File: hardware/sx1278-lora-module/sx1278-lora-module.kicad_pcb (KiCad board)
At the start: 2 copper layers, 17 x 16.5 mm, 1 part, among them J1 Conn_01x16

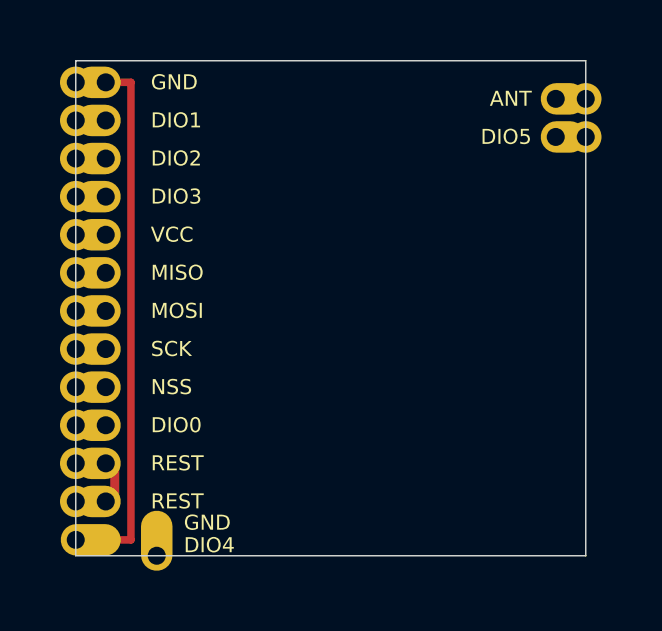
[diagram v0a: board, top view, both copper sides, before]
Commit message: SX1278 module: correct pad layout and pin names from the pinout photo
The seller's dimensioned pinout photo shows 12 keyhole pads along one
edge, two small castellation-only notches (DIO4, DIO5) on the adjacent
edge at the shared corner, and two keyhole pads (ANT, GND) at the
opposite corner.  Pin names in physical order are GND DIO1 DIO2 DIO3
VCC MISO MOSI SCK NSS DIO0 REST GND, DIO4 DIO5, GND ANT; the seller's
table duplicated REST and shifted its tail.  Positions re-measured
from the top-down photo: row holes 1.2 mm in from the edge starting
1.2 mm from the corner, notches at 1.25/2.7 mm, ANT/GND at 1.4/2.8 mm.

Co-Authored-By: Claude Fable 5.1 <noreply@anthropic.com>
Claude-Session: https://claude.ai/code/session_01JoGdh4Cg3VtTTDZi4gQuiN
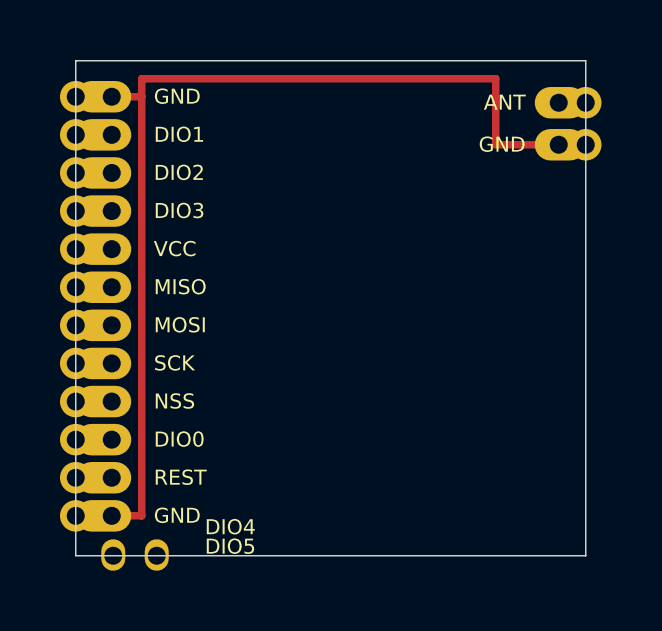
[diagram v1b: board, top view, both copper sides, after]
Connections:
- J1 pad 12: REST -> GND
- J1 pad 13: GND -> DIO4
- J1 pad 14: DIO4 -> DIO5
- J1 pad 15: DIO5 -> GND
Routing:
- net GND: track 16.3 -> 31.2 mm
- net REST: track 1.27 -> 0.00 mm
